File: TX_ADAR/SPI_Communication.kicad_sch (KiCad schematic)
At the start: 20 parts, among them SW1 SW_SPDT, U10 TXB0101DBV, U11 TXB0101DBV, U12 TXB0101DBV, U13 TXB0101DBV, U14 TXB0101DBV, U9 TXB0101DBV

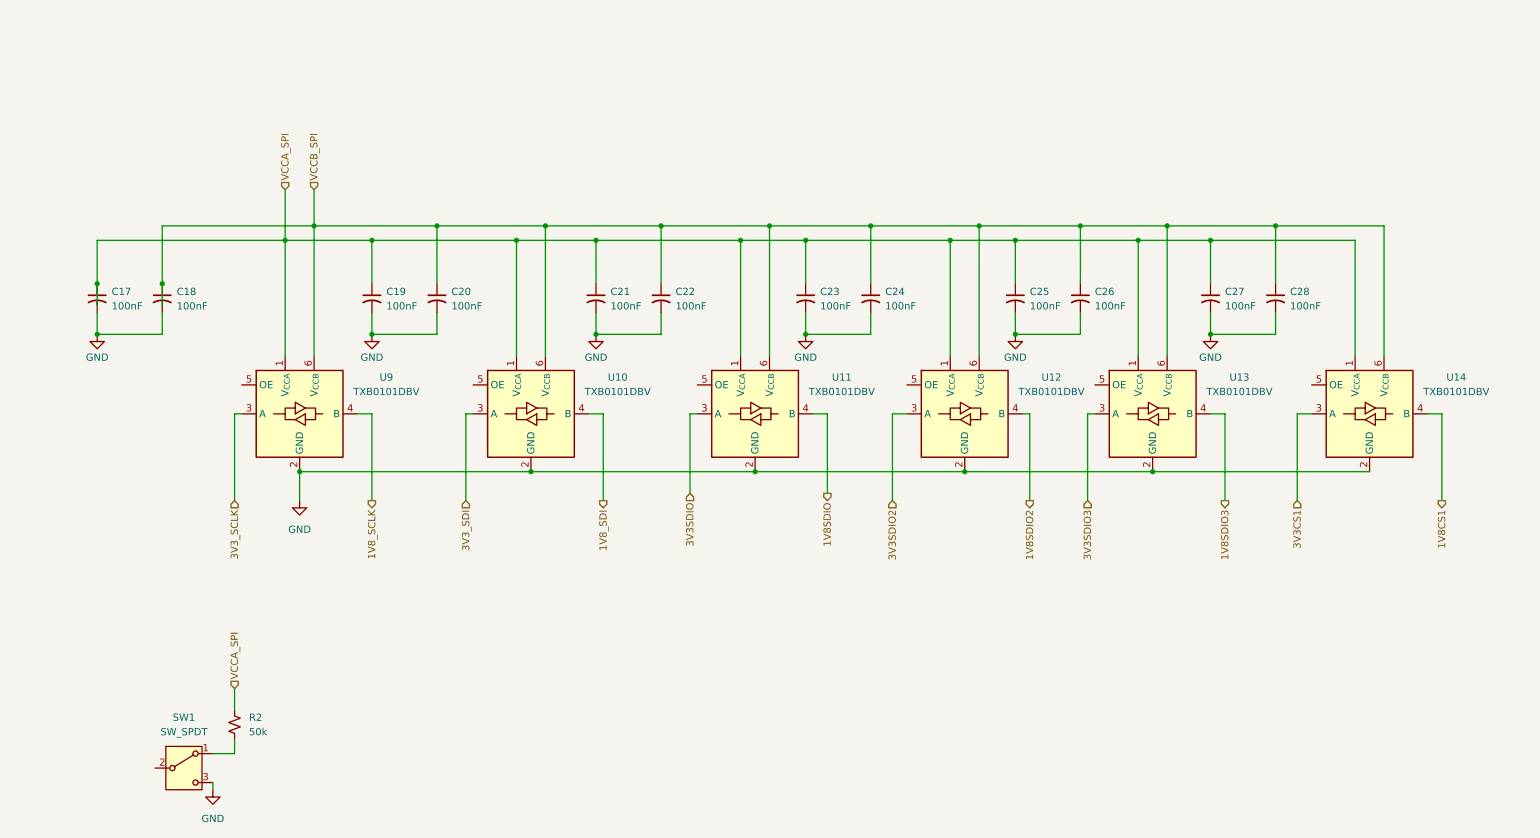
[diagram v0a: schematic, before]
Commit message: Cleaning up schematic
Added Cal Line
Connected RFOuts to connectors
Worked on State Machine connections
Finished connecting SDP Connector (need to double check)
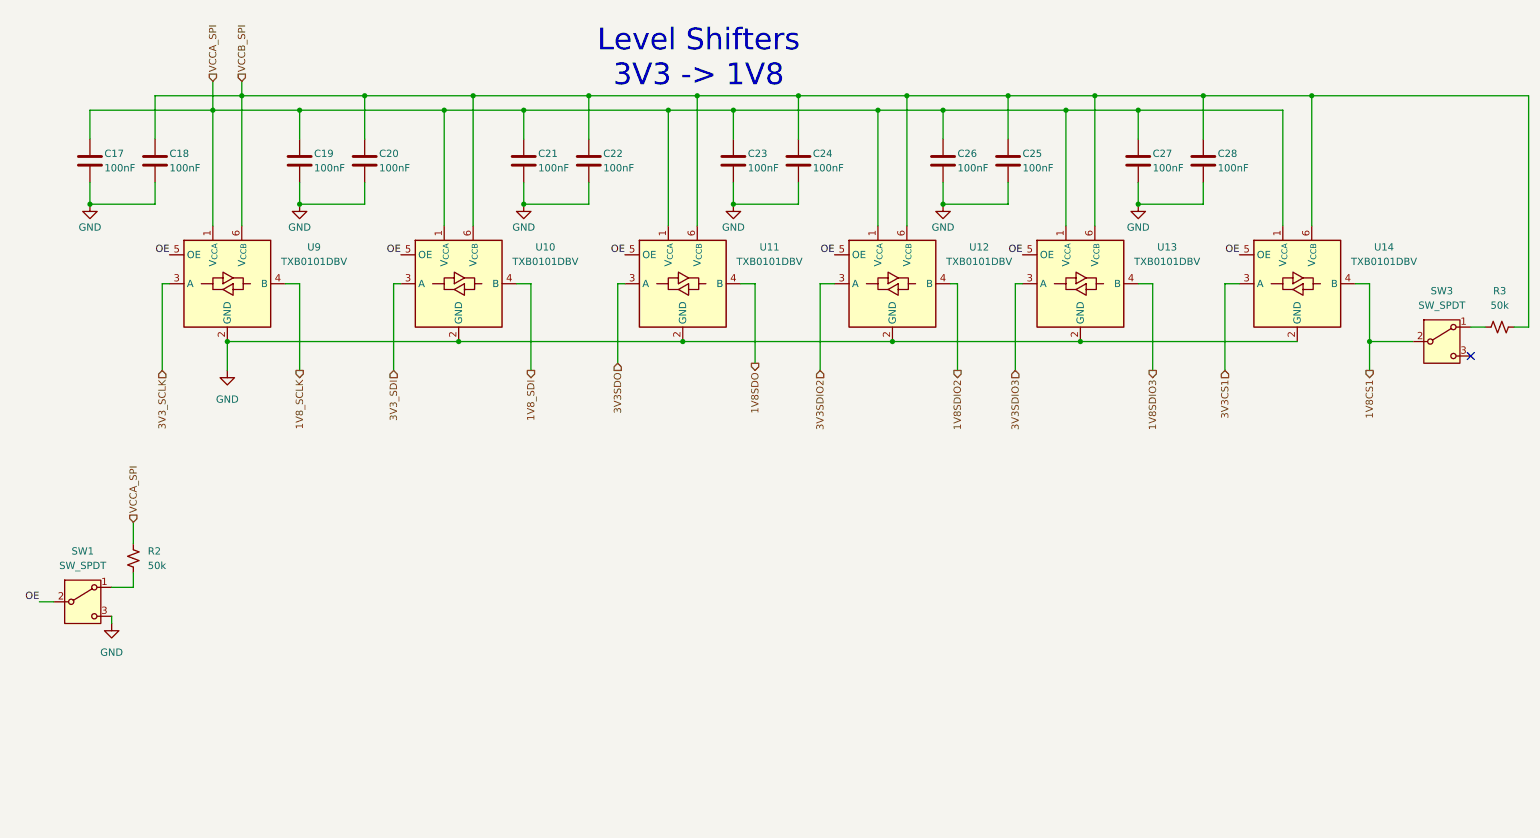
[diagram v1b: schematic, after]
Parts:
- removed C17, C18, C19, C20, C21, C22, C23, C24, C25, C26, C27, C28: 100nF, symbol Device:C_Small_US
- added C17, C18, C19, C20, C21, C22, C23, C24, C25, C26, C27, C28: 100nF, symbol Device:C
- added R3: 50k, symbol Device:R_Small_US
- added SW3: SW_SPDT, symbol Switch:SW_SPDT
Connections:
- net 1V8CS1: now also SW3.2 (B)
- net GND: now also C17.2, C18.2, C19.2, C20.2, C21.2, C22.2, C23.2, C24.2, C25.2, C26.2, C27.2, C28.2
- net VCCA_SPI: now also C17.1, C19.1, C21.1, C23.1, C26.1, C27.1
- net VCCB_SPI: now also C18.1, C20.1, C22.1, C24.1, C25.1, C28.1, R3.2
- net OE: now reaches U14.5 (OE)
- net OE: now also SW1.2 (B), U10.5 (OE), U11.5 (OE), U12.5 (OE), U13.5 (OE), U9.5 (OE)
- net 1V8SDIO renamed 1V8SDO
- net 3V3SDIO renamed 3V3SDO
- new net: R3.1, SW3.1 (A)
- no-connect marks 0 -> 1
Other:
- note added: "Level Shifters 3V3 -> 1V8"
- moved on the sheet: R2, SW1, U10, U11, U12, U13, U14, U9

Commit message: Running ERC
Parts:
- removed U9: TXB0101DBV, Package_TO_SOT_SMD:SOT-23-6, symbol Logic_LevelTranslator:TXB0101DBV
- added U19: TXB0101DBV, Package_TO_SOT_SMD:SOT-23-6, symbol Logic_LevelTranslator:TXB0101DBV
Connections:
- net 1V8_SCLK: now also U19.4 (B)
- net 3V3_SCLK: now also U19.3 (A)
- net GND: now also U19.2 (GND)
- net OE: now also U19.5 (OE)
- net VCCA_SPI: now also U19.1 (V_{CCA})
- net VCCB_SPI: now also U19.6 (V_{CCB})
- net 1V8CS1 renamed 1V8CSB
- net 3V3CS1 renamed 3V3CSB

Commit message: Fixed more issues
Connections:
- net VCCA_SPI: now also R3.2
- net VCCB_SPI: no longer R3.2
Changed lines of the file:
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@@
-	)
-	(junction
-		(at 241.3 26.67)
-		(diameter 0)
-		(color 0 0 0 0)
 	)
 	(junction
@@
 	(junction
 		(at 139.7 45.72)
+		(diameter 0)
+		(color 0 0 0 0)
+	)
+	(junction
+		(at 236.22 29.21)
 		(diameter 0)
 		(color 0 0 0 0)
@@
 	(wire
 		(pts
+			(xy 279.4 67.31) (xy 276.86 67.31)
+		)
+		(stroke
+			(width 0.254)
+			(type default)
+			(color 46 82 255 1)
+		)
+	)
+	(wire
+		(pts
 			(xy 170.18 26.67) (xy 170.18 49.53)
 		)
@@
 	(wire
 		(pts
+			(xy 279.4 29.21) (xy 279.4 67.31)
+		)
+		(stroke
+			(width 0.254)
+			(type default)
+			(color 46 82 255 1)
+		)
+	)
+	(wire
+		(pts
 			(xy 63.5 29.21) (xy 63.5 34.29)
 		)
@@
 	(wire
 		(pts
-			(xy 279.4 67.31) (xy 276.86 67.31)
-		)
-		(stroke
-			(width 0.254)
-			(type default)
-			(color 255 180 68 1)
-		)
-	)
-	(wire
-		(pts
 			(xy 88.9 29.21) (xy 88.9 49.53)
 		)
@@
 	(wire
 		(pts
-			(xy 241.3 26.67) (xy 279.4 26.67)
-		)
-		(stroke
-			(width 0.254)
-			(type default)
-			(color 255 180 68 1)
+			(xy 236.22 29.21) (xy 279.4 29.21)
+		)
+		(stroke
+			(width 0.254)
+			(type default)
+			(color 46 82 255 1)
 		)
 	)
@@
 		)
 		(stroke
-			(width 0.254)
-			(type default)
-			(color 255 180 68 1)
-		)
-	)
-	(wire
-		(pts
-			(xy 279.4 26.67) (xy 279.4 67.31)
-		)
-		(stroke

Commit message: Finished up adding footprints. Removed unnecessary switches for the TxRST and MRST
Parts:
- C17, C18, C19, C20, C21, C22, C23, C24, C25, C26, C27, C28: footprint (none) -> Capacitor_SMD:C_0603_1608Metric_Pad1.08x0.95mm_HandSolder
- R2, R3: footprint (none) -> Resistor_SMD:R_0603_1608Metric_Pad0.98x0.95mm_HandSolder
- SW1, SW3: footprint (none) -> 100SP1T1B4M2QE:SW_100SP1T1B4M2QE
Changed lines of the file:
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@@
 			)
 		)
-		(property "Footprint" ""
+		(property "Footprint" "Capacitor_SMD:C_0603_1608Metric_Pad1.08x0.95mm_HandSolder"
 			(at 27.6352 41.91 0)
 			(hide yes)
@@
 			)
 		)
-		(property "Footprint" ""
+		(property "Footprint" "100SP1T1B4M2QE:SW_100SP1T1B4M2QE"
 			(at 25.4 115.57 0)
 			(hide yes)
@@
 			)
 		)
-		(property "Footprint" ""
+		(property "Footprint" "Capacitor_SMD:C_0603_1608Metric_Pad1.08x0.95mm_HandSolder"
 			(at 211.7852 41.91 0)
 			(hide yes)
@@
 			)
 		)
-		(property "Footprint" ""
+		(property "Footprint" "Capacitor_SMD:C_0603_1608Metric_Pad1.08x0.95mm_HandSolder"
 			(at 115.2652 41.91 0)
 			(hide yes)
@@
 			)
 		)
-		(property "Footprint" ""
+		(property "Footprint" "Capacitor_SMD:C_0603_1608Metric_Pad1.08x0.95mm_HandSolder"
 			(at 177.4952 41.91 0)
 			(hide yes)
@@
 			)
 		)
-		(property "Footprint" ""
+		(property "Footprint" "Capacitor_SMD:C_0603_1608Metric_Pad1.08x0.95mm_HandSolder"
 			(at 188.9252 41.91 0)
 			(hide yes)
@@
 			)
 		)
-		(property "Footprint" ""
+		(property "Footprint" "100SP1T1B4M2QE:SW_100SP1T1B4M2QE"
 			(at 264.16 69.85 0)
 			(hide yes)
@@
 			)
 		)
-		(property "Footprint" ""
+		(property "Footprint" "Resistor_SMD:R_0603_1608Metric_Pad0.98x0.95mm_HandSolder"
 			(at 274.32 67.31 0)
 			(hide yes)
@@
 			)
 		)
-		(property "Footprint" ""
+		(property "Footprint" "Capacitor_SMD:C_0603_1608Metric_Pad1.08x0.95mm_HandSolder"
 			(at 39.0652 41.91 0)
 			(hide yes)
@@
 			)
 		)
-		(property "Footprint" ""
+		(property "Footprint" "Capacitor_SMD:C_0603_1608Metric_Pad1.08x0.95mm_HandSolder"
 			(at 140.6652 41.91 0)
 			(hide yes)
@@
 			)
 		)
-		(property "Footprint" ""
+		(property "Footprint" "Capacitor_SMD:C_0603_1608Metric_Pad1.08x0.95mm_HandSolder"
 			(at 223.2152 41.91 0)
 			(hide yes)
@@
 			)
 		)
-		(property "Footprint" ""
+		(property "Footprint" "Resistor_SMD:R_0603_1608Metric_Pad0.98x0.95mm_HandSolder"
 			(at 34.29 107.95 0)
 			(hide yes)
@@
 			)
 		)
-		(property "Footprint" ""
+		(property "Footprint" "Capacitor_SMD:C_0603_1608Metric_Pad1.08x0.95mm_HandSolder"
 			(at 64.4652 41.91 0)
 			(hide yes)
@@
 			)
 		)
-		(property "Footprint" ""
+		(property "Footprint" "Capacitor_SMD:C_0603_1608Metric_Pad1.08x0.95mm_HandSolder"
 			(at 152.0952 41.91 0)
 			(hide yes)
@@
 			)
 		)
-		(property "Footprint" ""
+		(property "Footprint" "Capacitor_SMD:C_0603_1608Metric_Pad1.08x0.95mm_HandSolder"
 			(at 75.8952 41.91 0)
 			(hide yes)
@@
 			)
 		)
-		(property "Footprint" ""
+		(property "Footprint" "Capacitor_SMD:C_0603_1608Metric_Pad1.08x0.95mm_HandSolder"
 			(at 103.8352 41.91 0)
 			(hide yes)

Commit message: Progress on layout
Rough idea of where each component will be relative to each other.
Had some ideas about a component that might be redundant.
Need to determine the final orientation of the components and size of pcb.
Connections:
- net 1V8CSB: now also U14.3 (A); no longer SW3.2 (B), U14.4 (B)
- net 1V8SDIO2: now also U12.3 (A); no longer U12.4 (B)
- net 1V8SDIO3: now also U13.3 (A); no longer U13.4 (B)
- net 1V8SDO: now also U11.3 (A); no longer U11.4 (B)
- net 1V8_SCLK: now also U19.3 (A); no longer U19.4 (B)
- net 1V8_SDI: now also U10.3 (A); no longer U10.4 (B)
- net 3V3CSB: now also SW3.2 (B), U14.4 (B); no longer U14.3 (A)
- net 3V3SDIO2: now also U12.4 (B); no longer U12.3 (A)
- net 3V3SDIO3: now also U13.4 (B); no longer U13.3 (A)
- net 3V3SDO: now also U11.4 (B); no longer U11.3 (A)
- net 3V3_SCLK: now also U19.4 (B); no longer U19.3 (A)
- net 3V3_SDI: now also U10.4 (B); no longer U10.3 (A)

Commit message: Layout Updates
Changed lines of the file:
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@@
-	)
-	(label "OE"
-		(at 17.78 115.57 180)
-		(effects
-			(font
-				(size 1.27 1.27)
-			)
-			(justify right bottom)
-		)
 	)
 	(label "OE"
@@
 		(effects
 			(font
+				(size 1.27 1.27)
+			)
+			(justify right)
+		)
+	)
+	(hierarchical_label "OE"
+		(shape output)
+		(at 17.78 115.57 180)
+		(effects
+			(font

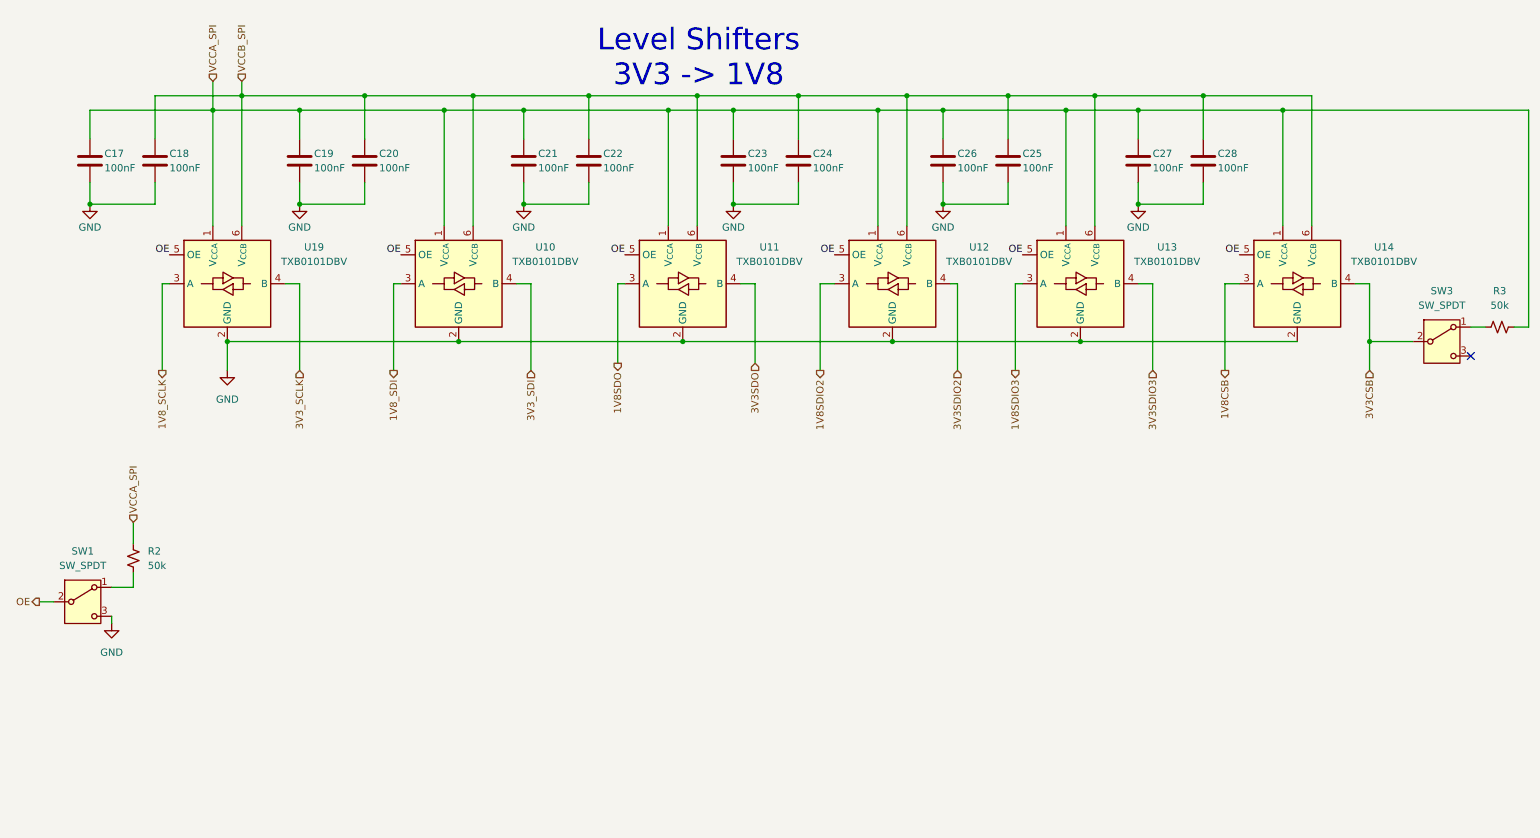
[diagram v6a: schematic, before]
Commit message: Got layout feedback from flatrim
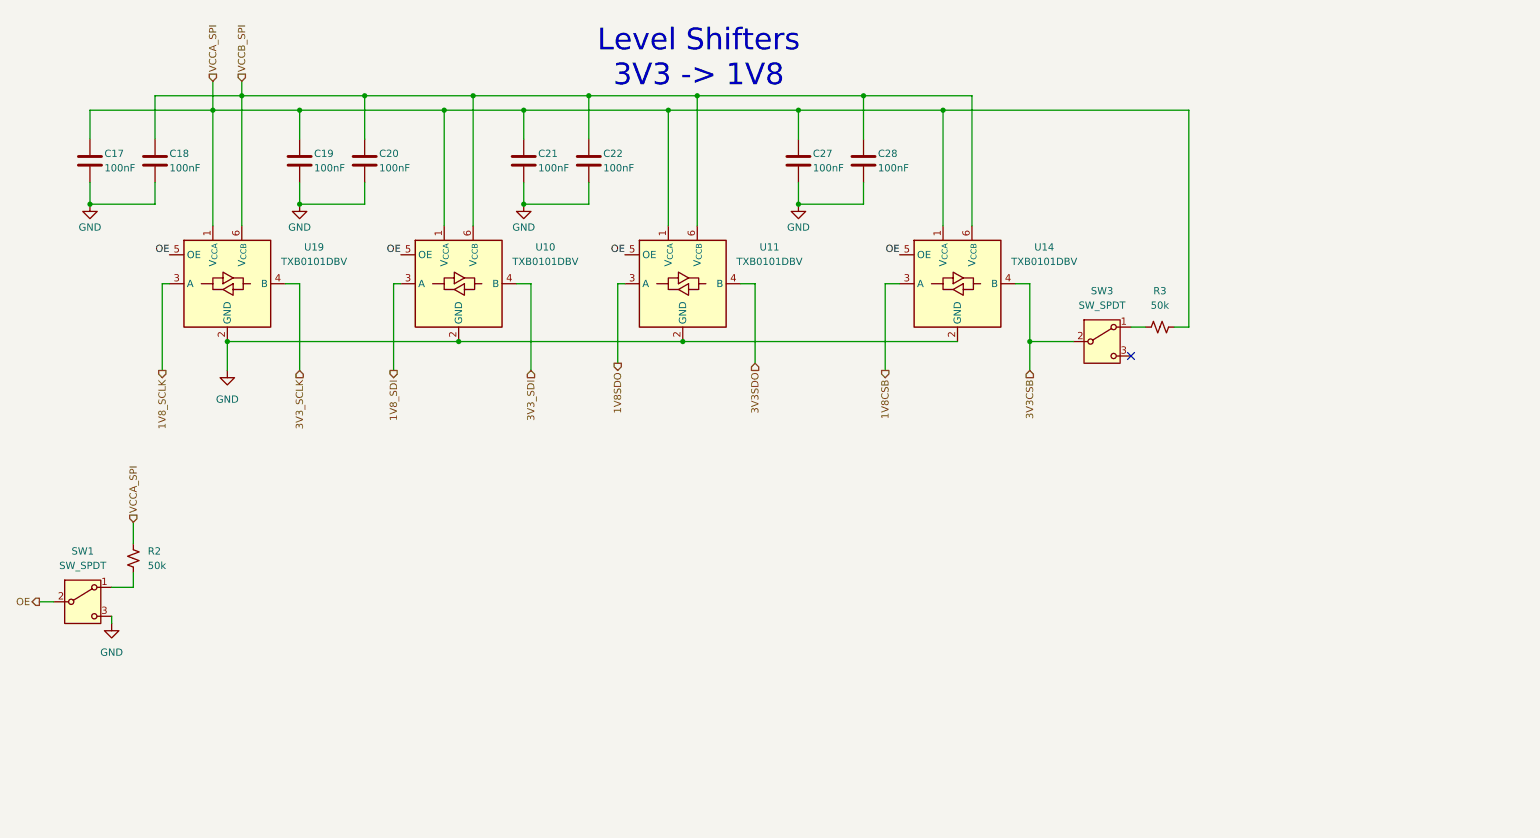
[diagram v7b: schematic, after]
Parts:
- removed C23, C24, C25, C26: 100nF, Capacitor_SMD:C_0603_1608Metric_Pad1.08x0.95mm_HandSolder, symbol Device:C
- removed U12, U13: TXB0101DBV, Package_TO_SOT_SMD:SOT-23-6, symbol Logic_LevelTranslator:TXB0101DBV
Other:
- moved on the sheet: C27, C28, R3, SW3, U14

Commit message: Added Level Shifters
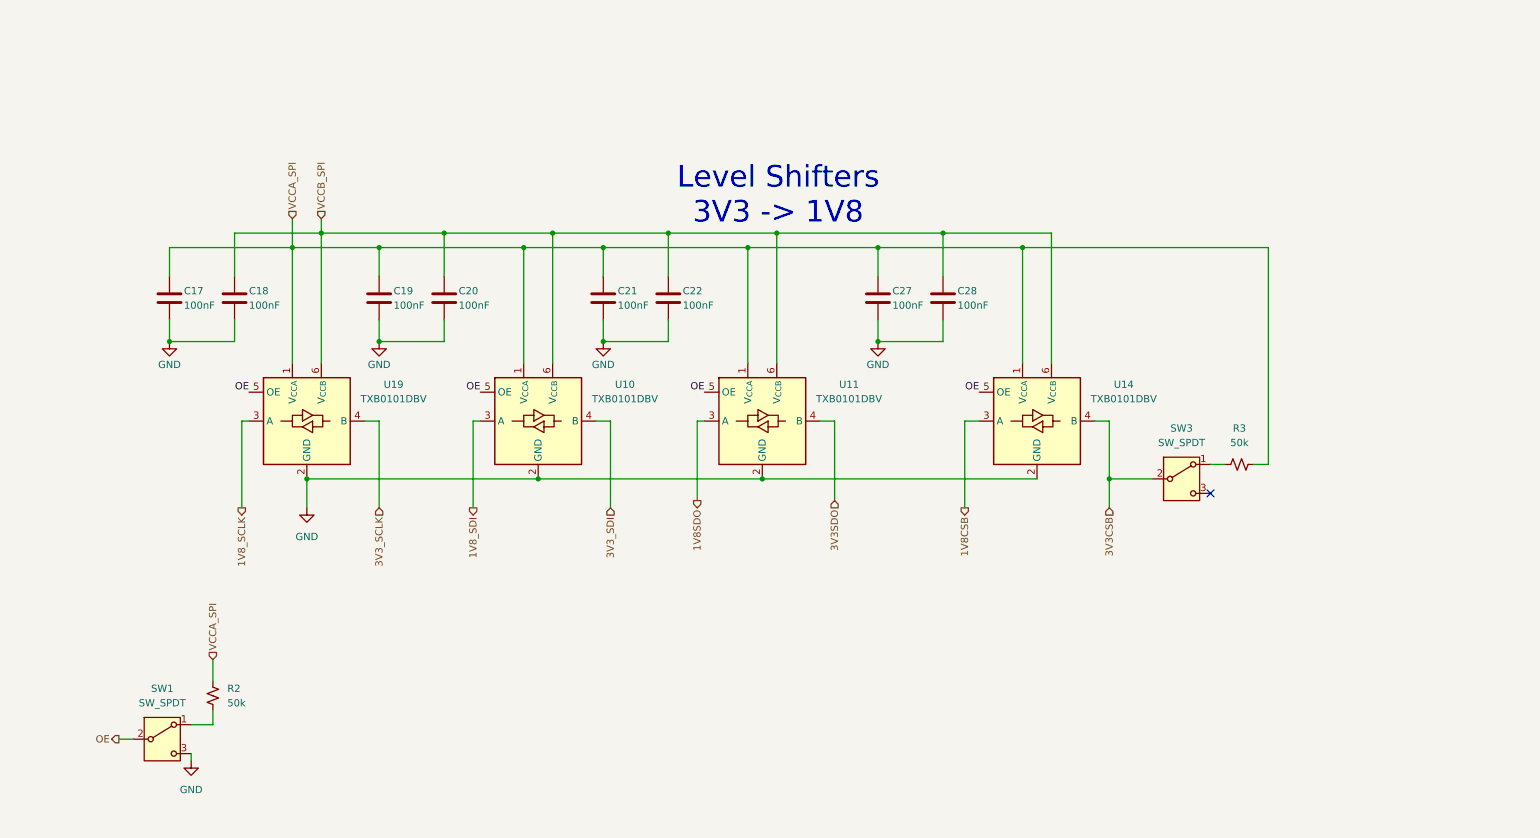
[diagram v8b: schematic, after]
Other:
- moved on the sheet: C17, C18, C19, C20, C21, C22, C27, C28, R2, R3, SW1, SW3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
